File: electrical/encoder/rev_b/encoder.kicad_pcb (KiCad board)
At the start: 2 copper layers, 14.8 x 48 mm, 5 parts, among them CN1 ENCODER;2xM1x3RA, Q1 AH1806;SC59, Q2 AH1806;SC59

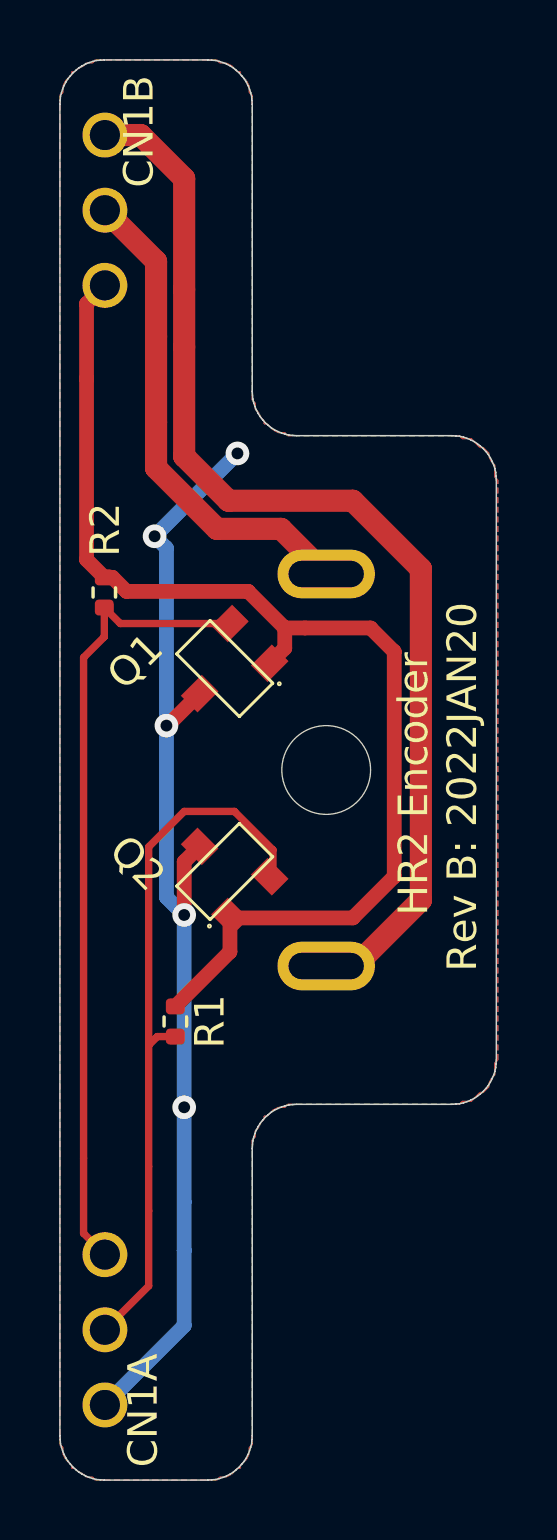
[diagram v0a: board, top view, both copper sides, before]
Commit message: Updated encoder/st-link Rev. B PCB's
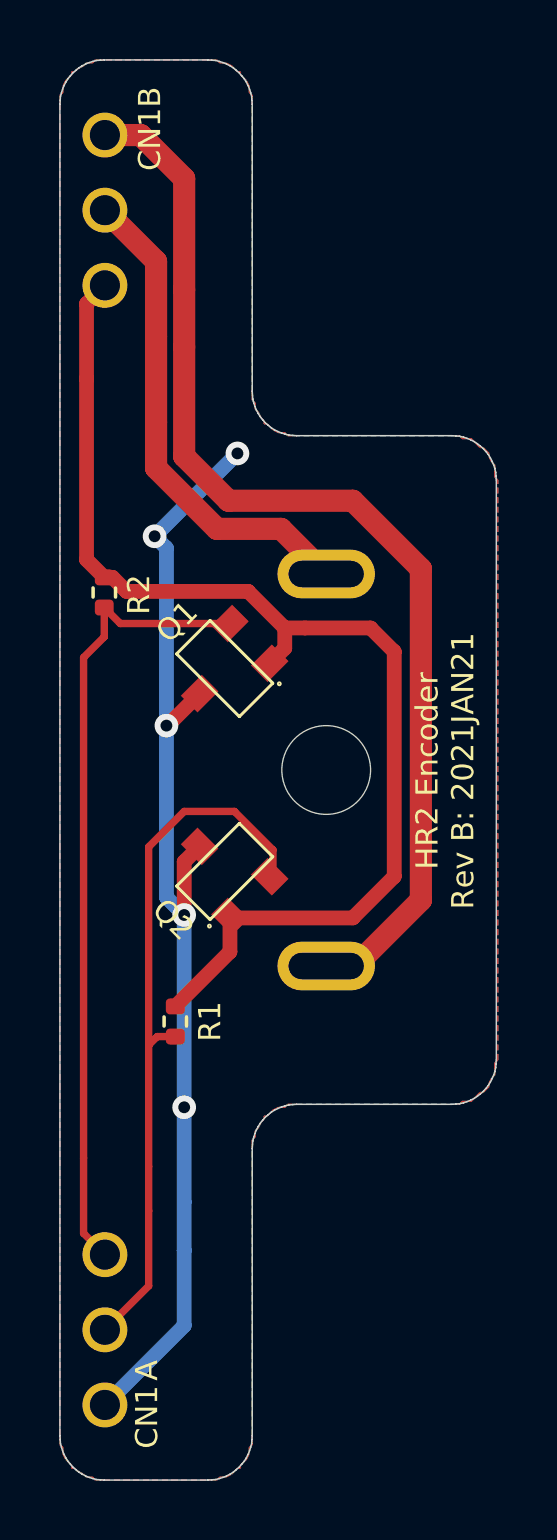
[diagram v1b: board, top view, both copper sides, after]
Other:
- board text added: "HR2 Encoder Rev B: 2021JAN21"
- board text removed: "HR2 Encoder"
- board text removed: "Rev B: 2022JAN20"
